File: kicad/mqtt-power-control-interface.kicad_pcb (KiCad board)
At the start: 2 copper layers, 16 parts, among them J1 Conn_01x04_Pin, J2 Conn_01x04_Pin, J3 Conn_01x04_Pin, J4 Conn_01x04_Pin, J5 Conn_01x04_Pin, J6 Conn_01x04_Pin, U1 LTV-847, U2 LTV-847, U3 LTV-847, U4 RPi Pico W

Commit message: Enhanced schematic and board
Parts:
- added J10: Conn_01x04_Pin, Connector_Molex:Molex_KK-254_AE-6410-04A_1x04_P2.54mm_Vertical, F.Cu at (120.7, 66.0)
- added J11: Conn_01x04_Pin, Connector_Molex:Molex_KK-254_AE-6410-04A_1x04_P2.54mm_Vertical, F.Cu at (120.7, 53.3)
- added J12: Conn_01x04_Pin, Connector_Molex:Molex_KK-254_AE-6410-04A_1x04_P2.54mm_Vertical, F.Cu at (120.7, 40.6)
- added J7: Conn_01x04_Pin, Connector_Molex:Molex_KK-254_AE-6410-04A_1x04_P2.54mm_Vertical, F.Cu at (120.7, 104.1)
- added J8: Conn_01x04_Pin, Connector_Molex:Molex_KK-254_AE-6410-04A_1x04_P2.54mm_Vertical, F.Cu at (120.7, 91.4)
- added J9: Conn_01x04_Pin, Connector_Molex:Molex_KK-254_AE-6410-04A_1x04_P2.54mm_Vertical, F.Cu at (120.7, 78.7)
- added R10: 330, Resistor_SMD:R_1206_3216Metric, B.Cu at (91.4, 74.9)
- added R11: 330, Resistor_SMD:R_1206_3216Metric, B.Cu at (91.6, 67.3)
- added R12: 330, Resistor_SMD:R_1206_3216Metric, B.Cu at (91.4, 59.7)
- added R7: 330, Resistor_SMD:R_1206_3216Metric, B.Cu at (63.3, 85.1)
- added R8: 330, Resistor_SMD:R_1206_3216Metric, B.Cu at (91.4, 87.6)
- added R9: 330, Resistor_SMD:R_1206_3216Metric, B.Cu at (91.4, 80.0)
- added U5: LTV-847, Package_DIP:DIP-16_W7.62mm, F.Cu at (109.2, 100.3)
- added U6: LTV-847, Package_DIP:DIP-16_W7.62mm, F.Cu at (109.2, 77.5)
- added U7: LTV-847, Package_DIP:DIP-16_W7.62mm, F.Cu at (109.2, 54.6)
- R1, R2, R3, R4, R5, R6: footprint Resistor_THT:R_Axial_DIN0204_L3.6mm_D1.6mm_P7.62mm_Horizontal -> Resistor_SMD:R_1206_3216Metric; moved to B.Cu
- U1: value LTV-847 -> RPi Pico W; footprint Package_DIP:DIP-16_W7.62mm -> Custom:RPI Pico W
- U4: value RPi Pico W -> LTV-847; footprint Custom:RPI Pico W -> Package_DIP:DIP-16_W7.62mm
- moved U4 132.4 mm to (45.7, 82.5)
- moved R1 89.3 mm to (63.3, 47.0)
- moved R2 89.3 mm to (63.3, 52.1)
- moved R3 89.3 mm to (63.3, 59.7)
- moved R4 89.3 mm to (63.3, 64.8)
- moved R5 89.3 mm to (63.3, 72.4)
- moved R6 89.3 mm to (63.3, 77.5)
- moved U3 84.4 mm to (45.7, 59.7)
- moved U2 82.7 mm to (45.7, 36.8)
- moved J6 77.6 mm to (34.3, 96.5)
- moved J5 77.6 mm to (34.3, 83.8)
- moved J4 77.5 mm to (34.3, 71.1)
- moved J3 77.5 mm to (34.3, 58.4)
- moved J2 77.5 mm to (34.3, 45.7)
- moved J1 77.5 mm to (34.3, 33.0)
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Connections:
- U1 pad 1: Net-(R1-Pad2) -> unconnected-(U1-GP0-Pad1)
- U1 pad 10: GPIO5 -> GPIO7
- U1 pad 11: DEV2_SW- -> GPIO8
- U1 pad 12: DEV2_SW+ -> GPIO9
- U1 pad 13: GND -> unconnected-(U1-GND3-Pad13)
- U1 pad 14: GPIO3 -> GPIO10
- U1 pad 15: DEV1_SW- -> GPIO11
- U1 pad 16: DEV1_SW+ -> GPIO12
- U1 pad 2: GND -> unconnected-(U1-GP1-Pad2)
- U1 pad 3: DEV1_LED+ -> GND
- U1 pad 4: DEV1_LED- -> GPIO2
- U1 pad 5: Net-(R2-Pad2) -> GPIO3
- U1 pad 6: GND -> GPIO4
- U1 pad 7: DEV2_LED+ -> GPIO5
- U1 pad 8: DEV2_LED- -> unconnected-(U1-GND2-Pad8)
- U1 pad 9: GND -> GPIO6
- U2 pad 1: Net-(R3-Pad2) -> Net-(R1-Pad2)
- U2 pad 10: GPIO9 -> GPIO5
- U2 pad 11: DEV4_SW- -> DEV2_SW-
- U2 pad 12: DEV4_SW+ -> DEV2_SW+
- U2 pad 14: GPIO7 -> GPIO3
- U2 pad 15: DEV3_SW- -> DEV1_SW-
- U2 pad 16: DEV3_SW+ -> DEV1_SW+
- U2 pad 3: DEV3_LED+ -> DEV1_LED+
- U2 pad 4: DEV3_LED- -> DEV1_LED-
- U2 pad 5: Net-(R4-Pad2) -> Net-(R2-Pad2)
- U2 pad 7: DEV4_LED+ -> DEV2_LED+
- U2 pad 8: DEV4_LED- -> DEV2_LED-
- U3 pad 1: Net-(R5-Pad2) -> Net-(R3-Pad2)
- U3 pad 10: GPIO13 -> GPIO9
- U3 pad 11: DEV6_SW- -> DEV4_SW-
- U3 pad 12: DEV6_SW+ -> DEV4_SW+
- U3 pad 14: GPIO11 -> GPIO7
- U3 pad 15: DEV5_SW- -> DEV3_SW-
- U3 pad 16: DEV5_SW+ -> DEV3_SW+
- U3 pad 3: DEV5_LED+ -> DEV3_LED+
- U3 pad 4: DEV5_LED- -> DEV3_LED-
- U3 pad 5: Net-(R6-Pad2) -> Net-(R4-Pad2)
- U3 pad 7: DEV6_LED+ -> DEV4_LED+
- U3 pad 8: DEV6_LED- -> DEV4_LED-
- U4 pad 1: unconnected-(U4-GP0-Pad1) -> Net-(R5-Pad2)
- U4 pad 10: GPIO7 -> GPIO13
- U4 pad 11: GPIO8 -> DEV6_SW-
- U4 pad 12: GPIO9 -> DEV6_SW+
- U4 pad 13: unconnected-(U4-GND3-Pad13) -> GND
- U4 pad 14: GPIO10 -> GPIO11
- U4 pad 15: GPIO11 -> DEV5_SW-
- U4 pad 16: GPIO12 -> DEV5_SW+
- U4 pad 2: unconnected-(U4-GP1-Pad2) -> GND
- U4 pad 3: GND -> DEV5_LED+
- U4 pad 4: GPIO2 -> DEV5_LED-
- U4 pad 5: GPIO3 -> Net-(R6-Pad2)
- U4 pad 6: GPIO4 -> GND
- U4 pad 7: GPIO5 -> DEV6_LED+
- U4 pad 8: unconnected-(U4-GND2-Pad8) -> DEV6_LED-
- U4 pad 9: GPIO6 -> GND
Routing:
- net Net-(R7-Pad2): track 0.00 -> 57.9 mm
- net GPIO15: track 0.00 -> 37.7 mm
- net GPIO13: track 0.00 -> 28.9 mm
- net Net-(R12-Pad2): track 0.00 -> 28.6 mm
- net Net-(R6-Pad2): track 0.00 -> 27.6 mm
- net GPIO28: track 0.00 -> 27.5 mm
- net Net-(R11-Pad2): track 0.00 -> 24.4 mm
- net GPIO26: track 0.00 -> 24.2 mm
- net GPIO11: track 0.00 -> 24.2 mm
- net Net-(R5-Pad2): track 0.00 -> 21.8 mm
- net GPIO21: track 0.00 -> 21.7 mm
- net DEV12_SW+: track 0.00 -> 20.6 mm
- net DEV12_SW-: track 0.00 -> 20.6 mm
- net DEV1_SW-: track 0.00 -> 20.6 mm
- net DEV1_SW+: track 0.00 -> 20.6 mm
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- added copper zone on B.Cu, net GND
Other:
- board outline added: 99.1 x 91.4 mm
- rule pad_to_mask_clearance: 0 -> 0.038
- board text added: "BTN+"
- board text added: "BTN-"
- board text added: "JLCJLCJLCJLC"
- board text added: "LED+"
- board text added: "LED-"
- board text added: "mqtt-power-control-interface v1.0.0"

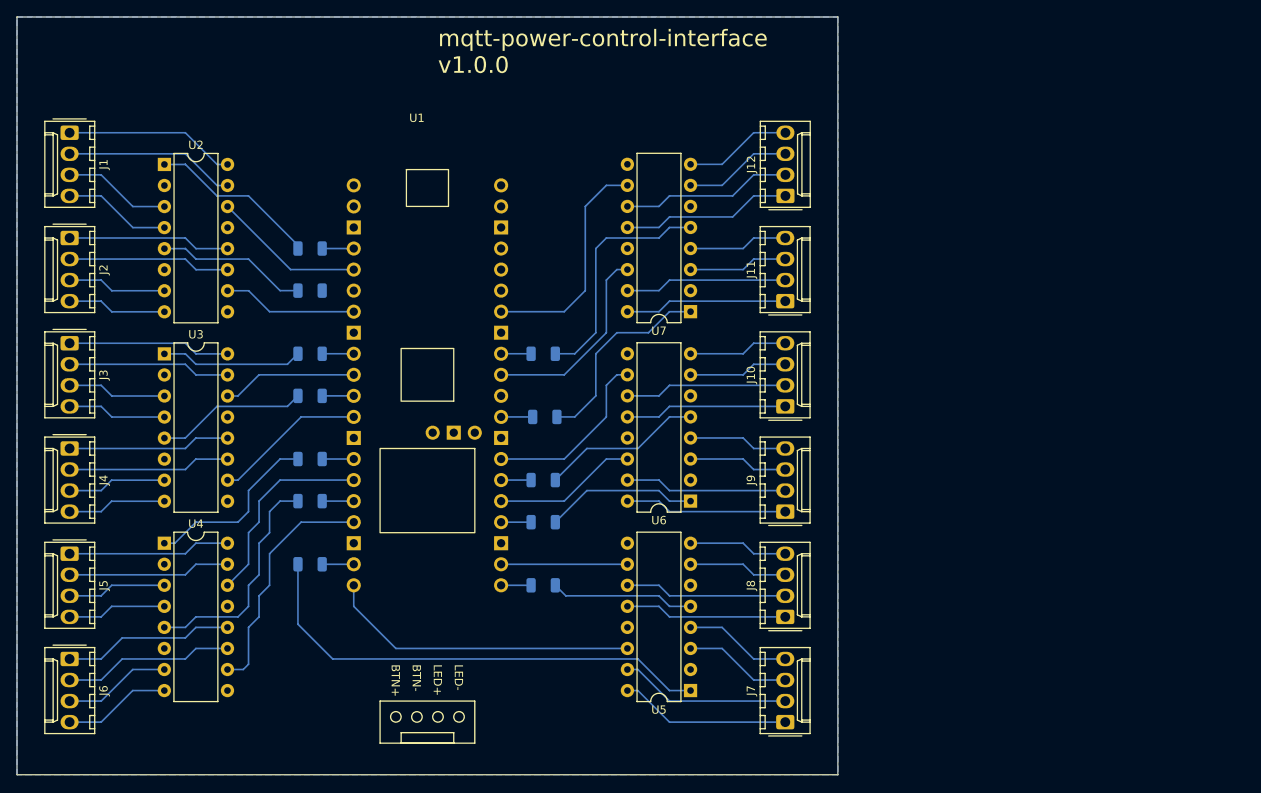
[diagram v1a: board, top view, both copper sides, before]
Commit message: Updated board, using THT resistors, fixed wiring
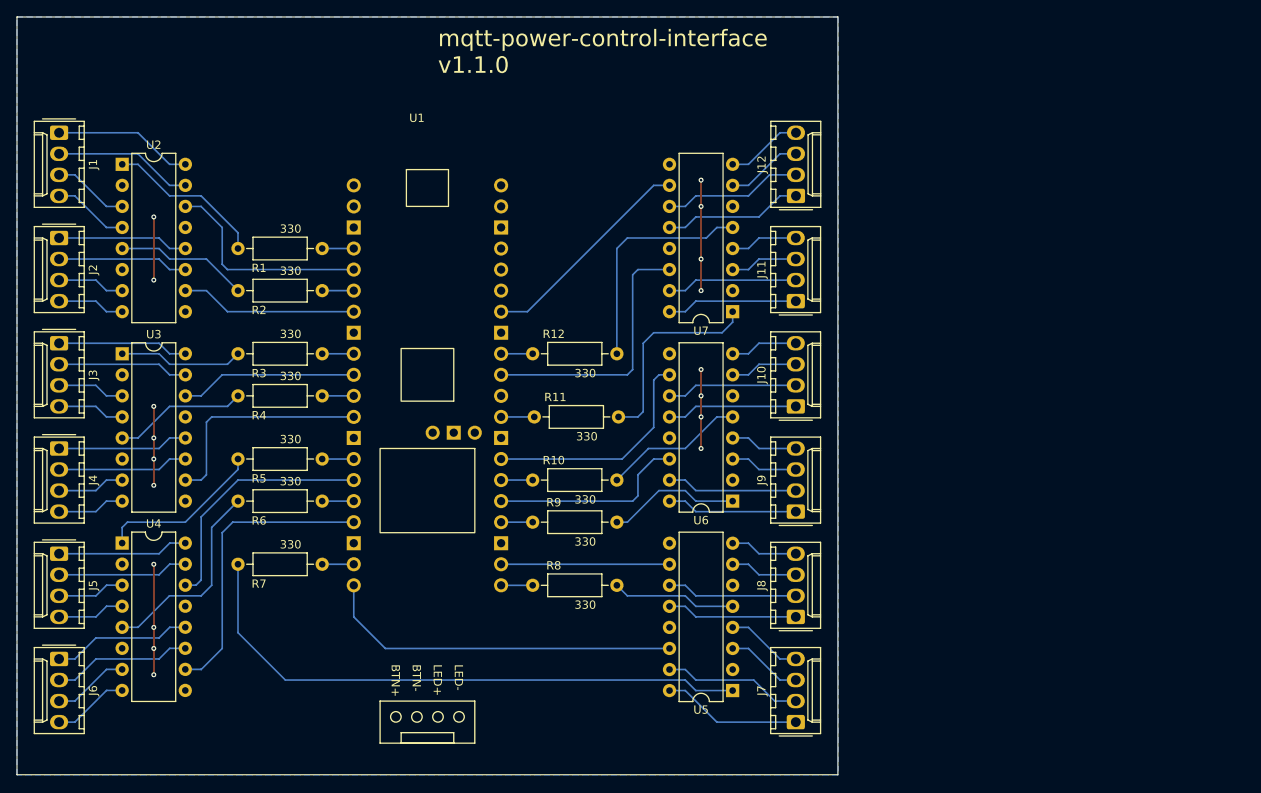
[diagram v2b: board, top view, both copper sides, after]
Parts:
- R1, R10, R11, R12, R2, R3, R4, R5, R6, R7, R8, R9: footprint Resistor_SMD:R_1206_3216Metric -> Resistor_THT:R_Axial_DIN0207_L6.3mm_D2.5mm_P10.16mm_Horizontal; moved to F.Cu
- moved U2 5.09 mm to (40.6, 36.8)
- moved U3 5.09 mm to (40.6, 59.7)
- moved U4 5.09 mm to (40.6, 82.5)
- moved U5 5.08 mm to (114.3, 100.3)
- moved U6 5.08 mm to (114.3, 77.5)
- moved U7 5.08 mm to (114.3, 54.6)
- moved R1 1.46 mm to (64.8, 47.0)
- moved R2 1.46 mm to (64.8, 52.1)
- moved R3 1.46 mm to (64.8, 59.7)
- moved R4 1.46 mm to (64.8, 64.8)
- moved R5 1.46 mm to (64.8, 72.4)
- moved R6 1.46 mm to (64.8, 77.5)
- moved R7 1.46 mm to (64.8, 85.1)
- moved J1 1.27 mm to (33.0, 33.0)
- moved J10 1.27 mm to (121.9, 66.0)
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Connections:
- U1 pad 13: unconnected-(U1-GND3-Pad13) -> GND
- U1 pad 18: unconnected-(U1-GND4-Pad18) -> GND
- U1 pad 23: unconnected-(U1-GND5-Pad23) -> GND
- U1 pad 28: unconnected-(U1-GND6-Pad28) -> GND
- U1 pad 33: unconnected-(U1-GND7-Pad33) -> GND
- U1 pad 42: unconnected-(U1-GND_DEBUG-Pad42) -> GND
- U1 pad 8: unconnected-(U1-GND2-Pad8) -> GND
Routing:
- net GND: track 0.00 -> 53.3 mm, vias 0 -> 18
- net Net-(R7-Pad2): track 57.9 -> 70.8 mm
- net GPIO9: track 18.4 -> 27.2 mm
- net GPIO26: track 24.2 -> 32.3 mm
- net GPIO3: track 18.4 -> 26.1 mm
- net GPIO13: track 28.9 -> 35.9 mm
- net GPIO19: track 17.3 -> 23.9 mm
- net GPIO21: track 21.7 -> 27.9 mm
- net GPIO11: track 24.2 -> 30.0 mm
- net GPIO15: track 37.7 -> 43.5 mm
- net GPIO5: track 16.3 -> 21.4 mm
- net GPIO7: track 16.3 -> 21.4 mm
- net GPIO17: track 15.2 -> 20.3 mm
- net DEV2_SW-: track 19.6 -> 15.8 mm
- net DEV2_SW+: track 19.6 -> 15.8 mm
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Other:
- board text added: "mqtt-power-control-interface v1.1.0"
- board text removed: "mqtt-power-control-interface v1.0.0"
